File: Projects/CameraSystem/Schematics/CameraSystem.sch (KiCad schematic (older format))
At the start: 0 parts

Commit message: linux adaptation
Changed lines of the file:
@@
 F4 "SD_SCK" I R 1750 5550 60
 F5 "_SD_CS" I R 1750 5800 60
-F6 "SD_MISO" O R 1750 5300 60
-F7 "SD_MOSI" I R 1750 5050 60
+F6 "SD_DATA_IN_BUF" I R 1750 5050 60
+F7 "SD_DATA_OUT_BUF" O R 1750 5300 60
 $EndSheet
 Wire Wire Line

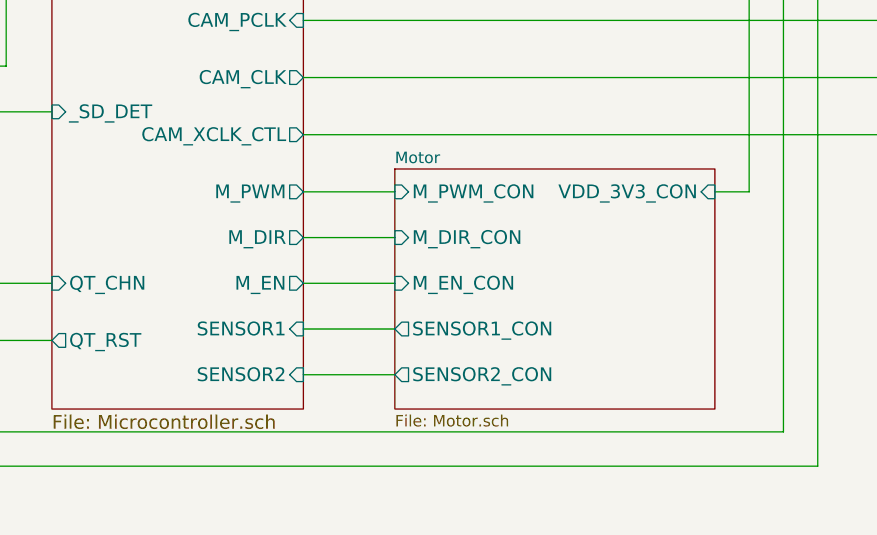
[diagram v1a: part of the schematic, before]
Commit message: camera was updated
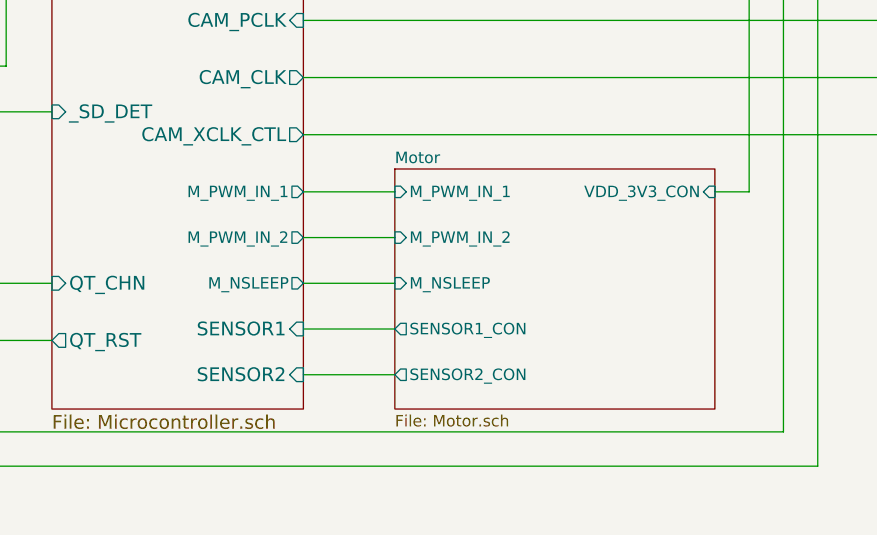
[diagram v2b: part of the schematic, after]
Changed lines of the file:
@@
 EESchema Schematic File Version 4
 LIBS:CameraSystem-cache
-EELAYER 26 0
+EELAYER 29 0
 EELAYER END
 $Descr A4 11693 8268
@@
 F23 "CAM_XCLK_CTL" O R 4550 6100 60
 F24 "QT_RST" O L 3450 7000 60
-F25 "M_PWM" O R 4550 6350 60
-F26 "M_DIR" O R 4550 6550 60
-F27 "M_EN" O R 4550 6750 60
-F28 "SENSOR1" I R 4550 6950 60
-F29 "SENSOR2" I R 4550 7150 60
-F30 "_SD_DET" I L 3450 6000 60
-F31 "QT_CHN" I L 3450 6750 60
-F32 "UC_SPI_TX" O L 3450 2500 50
-F33 "UC_SPI_RX" I L 3450 2200 50
-F34 "U2_SPI_RST" I L 3450 1900 50
+F25 "SENSOR1" I R 4550 6950 60
+F26 "SENSOR2" I R 4550 7150 60
+F27 "_SD_DET" I L 3450 6000 60
+F28 "QT_CHN" I L 3450 6750 60
+F29 "UC_SPI_TX" O L 3450 2500 50
+F30 "UC_SPI_RX" I L 3450 2200 50
+F31 "U2_SPI_RST" I L 3450 1900 50
+F32 "M_NSLEEP" O R 4550 6750 50
+F33 "M_PWM_IN_1" O R 4550 6350 50
+F34 "M_PWM_IN_2" O R 4550 6550 50
 $EndSheet
 $Sheet
@@
 Text Notes 8900 1650 0    60   ~ 0
 To be done:\n1. Add debug ping in all communication lines
-$Sheet
-S 4950 6250 1400 1050
-U 5BC611AE
-F0 "Motor" 50
-F1 "Motor.sch" 50
-F2 "VDD_3V3_CON" I R 6350 6350 60
-F3 "M_PWM_CON" I L 4950 6350 60
-F4 "M_DIR_CON" I L 4950 6550 60
-F5 "M_EN_CON" I L 4950 6750 60
-F6 "SENSOR1_CON" O L 4950 6950 60
-F7 "SENSOR2_CON" O L 4950 7150 60
-$EndSheet
 Wire Wire Line
 	4950 6350 4550 6350
@@
 Wire Wire Line
 	2950 5300 1750 5300
+$Sheet
+S 4950 6250 1400 1050
+U 5BC611AE
+F0 "Motor" 50
+F1 "Motor.sch" 50
+F2 "VDD_3V3_CON" I R 6350 6350 50
+F3 "M_PWM_IN_1" I L 4950 6350 50
+F4 "M_PWM_IN_2" I L 4950 6550 50
+F5 "M_NSLEEP" I L 4950 6750 50
+F6 "SENSOR1_CON" O L 4950 6950 50
+F7 "SENSOR2_CON" O L 4950 7150 50
+$EndSheet
 $EndSCHEMATC
